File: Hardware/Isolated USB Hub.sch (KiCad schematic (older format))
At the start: 76 parts, among them J1 PWR_IN, J2 USB_US, J3 USB_A_Double, J4 USB_A_Double, J5 USB_A_Double, J6 HUB_PROG, U10 USBLC6-2SC6, U11 USBLC6-2SC6, U12 USBLC6-2SC6, U13 USBLC6-2SC6, U14 24LC02BT-I_OT, U15 USBLC6-2SC6, U2 USBLC6-2SC6, U3 LF33_TO252, U4 USB2513B_Bi, U5 NMUSB202MC-R7, U6 NMUSB202MC-R7, U7 NMUSB202MC-R7, U9 USBLC6-2SC6, Y1 Crystal

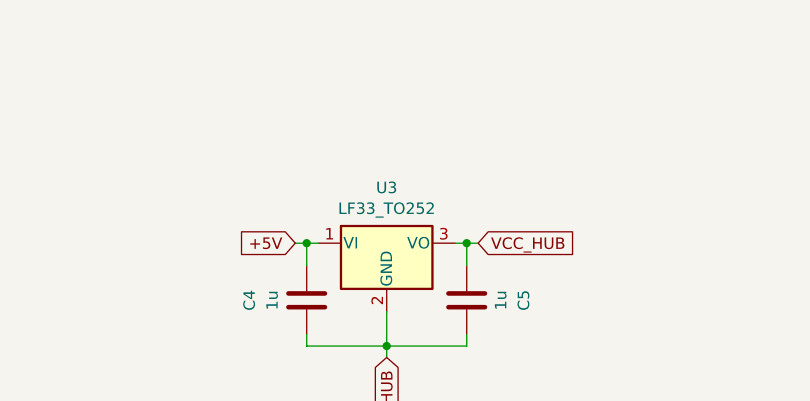
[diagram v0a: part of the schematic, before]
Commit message: Add power LED
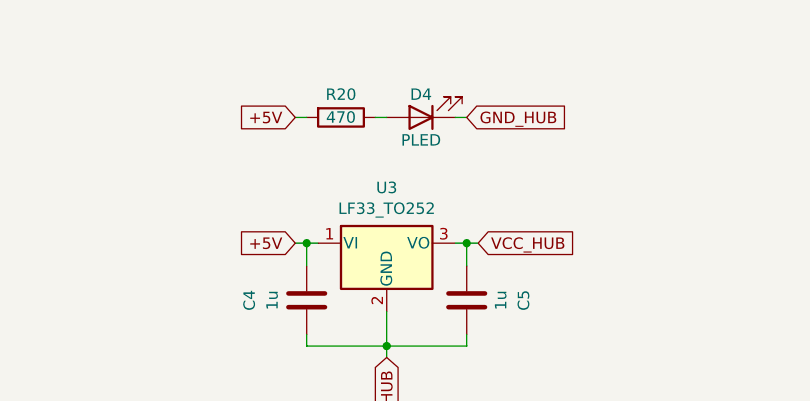
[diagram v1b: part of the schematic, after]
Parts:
- added D4: PLED, Pin_Headers:Pin_Header_Straight_1x02_Pitch2.54mm, symbol Device:LED
- added R20: 470, Resistors_SMD:R_0805, symbol Device:R
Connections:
- net +5V: now also R20.2
- net GND_HUB: now also D4.1 (K)
- new net: D4.2 (A), R20.1
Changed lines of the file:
@@
 EESchema Schematic File Version 4
-LIBS:Isolated USB Hub-cache
 EELAYER 30 0
 EELAYER END
@@
 Wire Wire Line
 	14350 12500 14350 12550
+$Comp
+L Device:LED D4
+U 1 1 5FE52A0B
+P 4000 1300
+F 0 "D4" H 4000 1200 50  0000 C CNN
+F 1 "PLED" H 4000 1400 50  0000 C CNN
+F 2 "Pin_Headers:Pin_Header_Straight_1x02_Pitch2.54mm" H 4000 1300 50  0001 C CNN
+F 3 "~" H 4000 1300 50  0001 C CNN
+	1    4000 1300
+	-1   0    0    1
+$EndComp
+Text GLabel 3450 1300 0    50   Input ~ 0
++5V
+Text GLabel 4200 1300 2    50   Input ~ 0
+GND_HUB
+$Comp
+L Device:R R20
+U 1 1 5FE6C3A1
+P 3650 1300
+F 0 "R20" V 3550 1300 50  0000 C CNN
+F 1 "470" V 3650 1300 50  0000 C CNN
+F 2 "Resistors_SMD:R_0805" V 3580 1300 50  0001 C CNN
+F 3 "~" H 3650 1300 50  0001 C CNN
+	1    3650 1300
+	0    1    1    0
+$EndComp
+Wire Wire Line
+	3450 1300 3500 1300
+Wire Wire Line
+	3800 1300 3850 1300
+Wire Wire Line
+	4150 1300 4200 1300
 $EndSCHEMATC
